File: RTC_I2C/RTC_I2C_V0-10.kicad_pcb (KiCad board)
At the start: 2 copper layers, 17 parts, among them K1 CONN_1, K2 COLONETTE, K3 COLONETTE, K4 COLONETTE, K5 COLONETTE, K6 CONN_1, P1 CONN_4, U1 PCF8563, X1 CRYSTAL

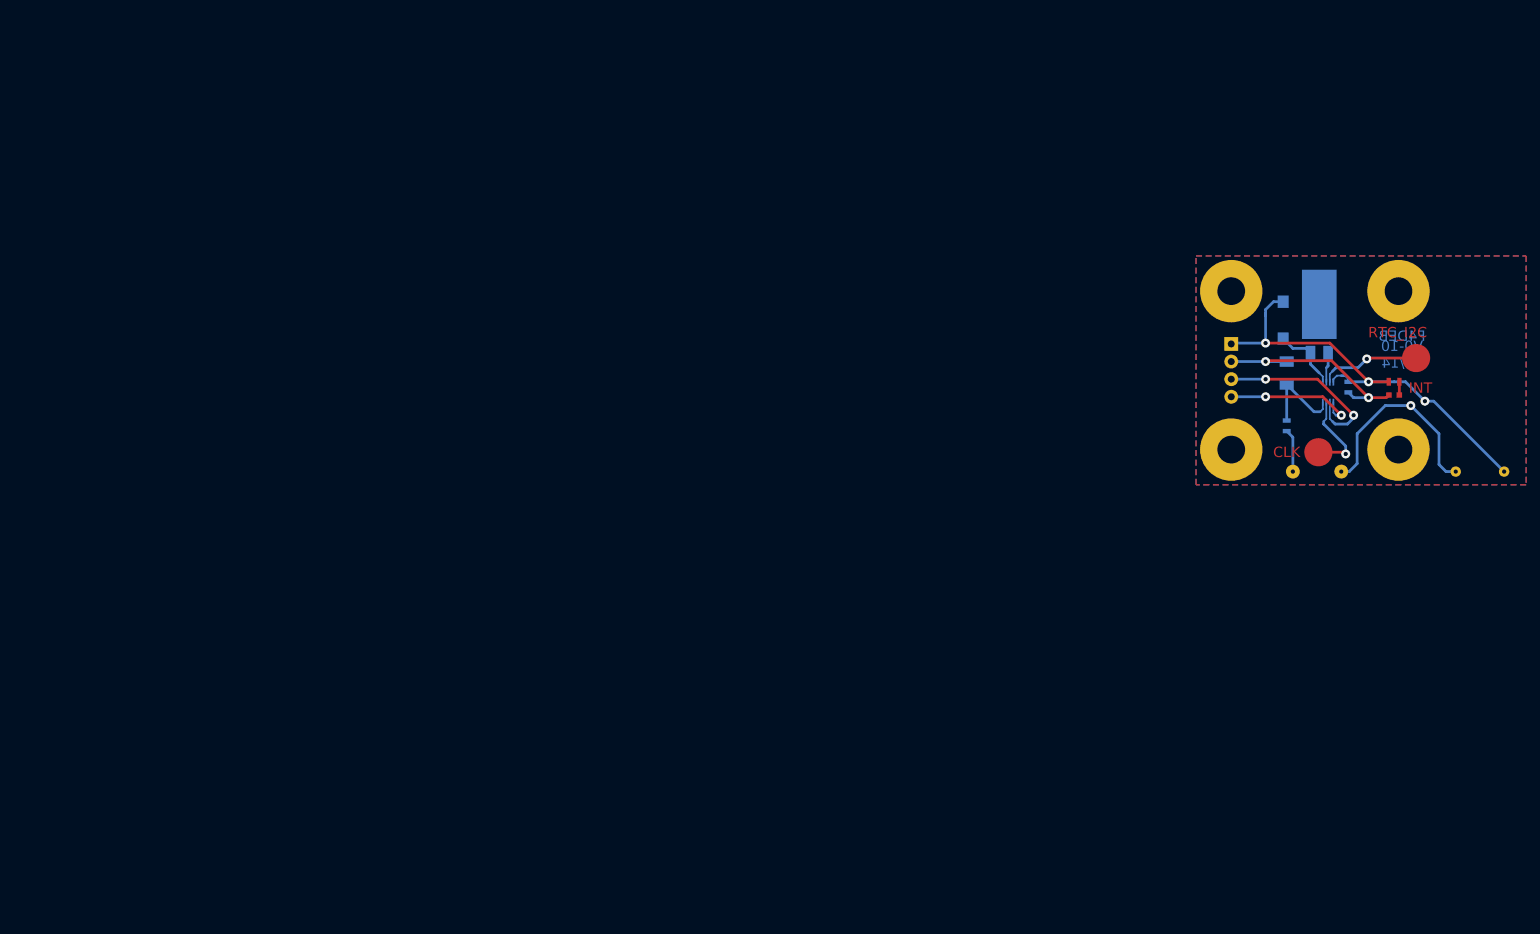
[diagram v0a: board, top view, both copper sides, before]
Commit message: Modification for printing
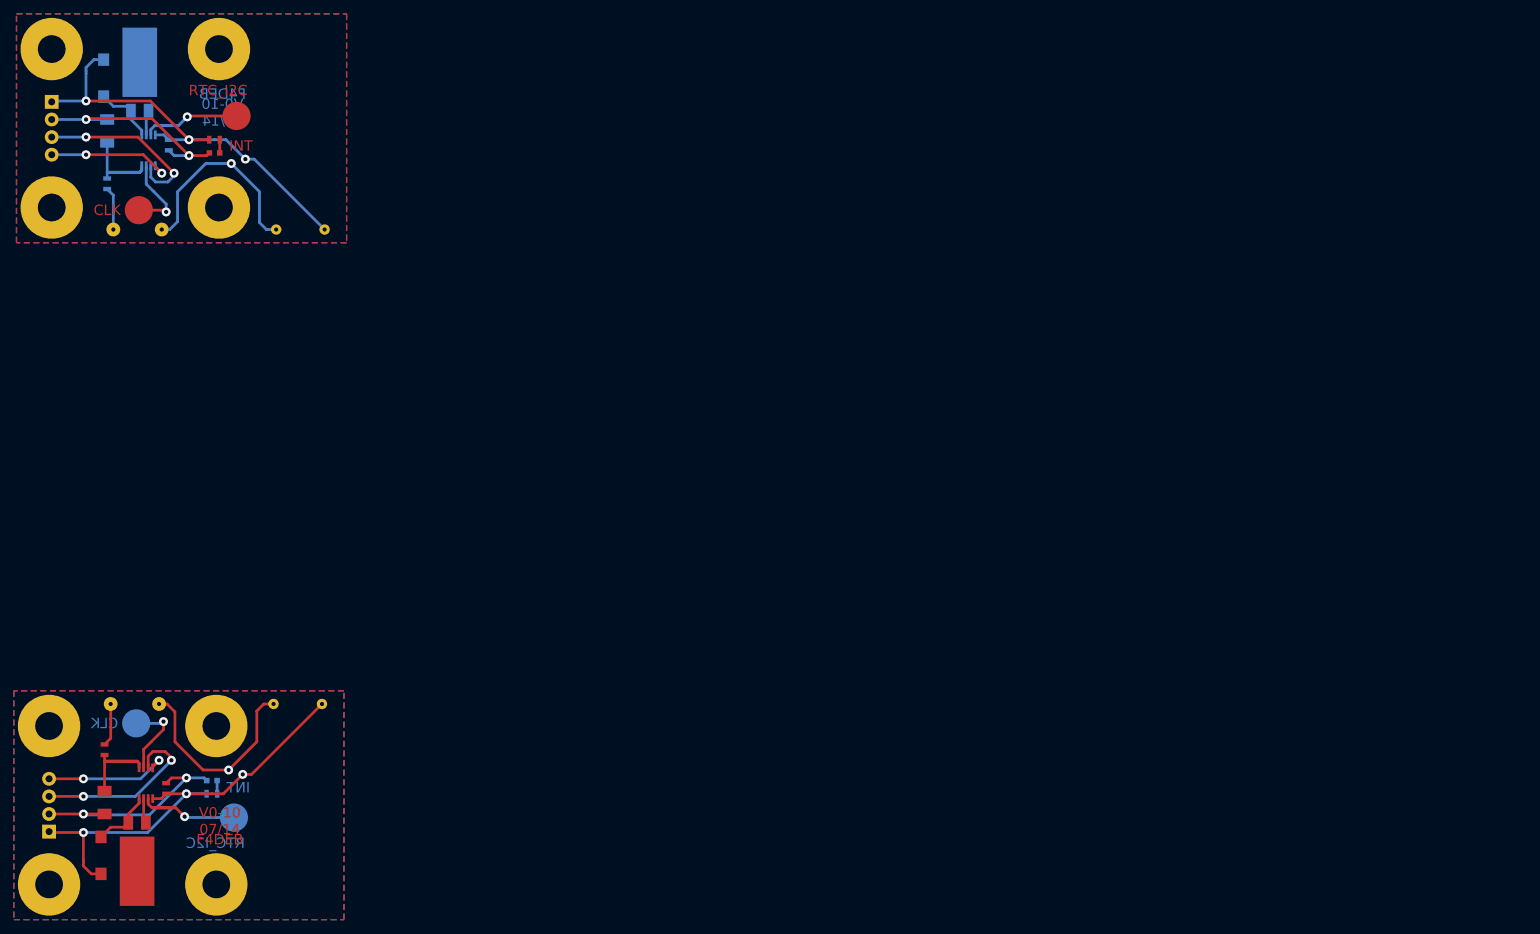
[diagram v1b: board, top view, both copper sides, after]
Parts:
- added C1: 10F/2.7V, C-10F, B.Cu at (77.7, 134.5)
- added C2: 10p, CAJCMS, F.Cu at (43.3, 155.2)
- added C3: 10F/2.7V, C-10F, B.Cu at (54.2, 134.5)
- added C4: 100n, SM0603_Capa, F.Cu at (52.7, 142.9)
- added D1: DIODESCH, SM1206, F.Cu at (43.8, 144.9)
- added D2: VERT, LED-0603, B.Cu at (59.3, 141.7)
- added K1: CONN_1, 1pin, B.Cu at (48.4, 133.5)
- added K2: COLONETTE, COLONETTE, B.Cu at (35.8, 156.7)
- added K3: COLONETTE, COLONETTE, B.Cu at (59.9, 156.7)
- added K4: COLONETTE, COLONETTE, B.Cu at (35.8, 133.9)
- added K5: COLONETTE, COLONETTE, B.Cu at (59.9, 133.9)
- added K6: CONN_1, 1pin, B.Cu at (62.5, 147.1)
- added P1: CONN_4, KK-4, B.Cu at (35.8, 141.5)
- added R1: 150, SM0603_Resistor, F.Cu at (43.8, 137.3)
- added R2: 1K, SM0603_Resistor, B.Cu at (59.3, 143.6)
- added U1: PCF8563, SSOP8, F.Cu at (49.8, 142.1)
- added X1: CRYSTAL, QTZ32KHZ, F.Cu at (49.8, 151.0)
- U1: footprint VSSOP-8 -> SSOP8
- moved C1 173.7 mm to (78.1, 58.4)
- moved C2 173.7 mm to (43.7, 37.7)
- moved C3 173.7 mm to (54.6, 58.4)
- moved C4 173.7 mm to (53.1, 50.0)
- moved D1 173.7 mm to (44.2, 48.0)
- moved D2 173.7 mm to (59.7, 51.2)
- moved K1 173.7 mm to (48.8, 59.4)
- moved K2 173.7 mm to (36.2, 36.2)
- moved K3 173.7 mm to (60.3, 36.2)
- moved K4 173.7 mm to (36.2, 59.1)
- moved K5 173.7 mm to (60.3, 59.1)
- moved P1 173.7 mm to (36.2, 51.4)
- moved R1 173.7 mm to (44.2, 55.6)
- moved R2 173.7 mm to (59.7, 49.3)
- moved U1 173.7 mm to (50.2, 50.8), turned to 0 degrees
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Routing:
- net GND: track 64.3 -> 126.0 mm, vias 3 -> 6
- net N-000004: track 58.1 -> 116.1 mm, vias 1 -> 2
- net +5VD: track 31.5 -> 62.9 mm, vias 2 -> 4
- net /SCL: track 26.7 -> 51.7 mm, vias 2 -> 4
- net /INT: track 19.6 -> 43.2 mm, vias 1 -> 2
- net /SDA: track 19.8 -> 39.5 mm, vias 2 -> 4
- net N-000005: track 13.4 -> 31.7 mm
- net /CLKO: track 13.0 -> 23.8 mm, vias 1 -> 2
- net N-0000011: track 11.6 -> 17.8 mm
- net N-000003: track 6.21 -> 12.4 mm
- net N-0000010: track 4.71 -> 7.26 mm
- net N-000001: track 1.91 -> 3.82 mm
